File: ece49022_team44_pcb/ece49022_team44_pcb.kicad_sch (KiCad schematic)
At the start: 75 parts, among them J1 Conn_02x05_Odd_Even, J3 Conn_01x05_Female, J4 Conn_01x04_Female, J5 Conn_01x06_Female, Q1 MMBT3904, SW1 RotaryEncoder_Switch, SW2 Reset, U1 STM32F091RCTx, U2 HDC1080, U3 CR2013-MI2120, U4 PCA9306DC, U5 PCF8523T, U6 MAX30102, U7 MPU-6050

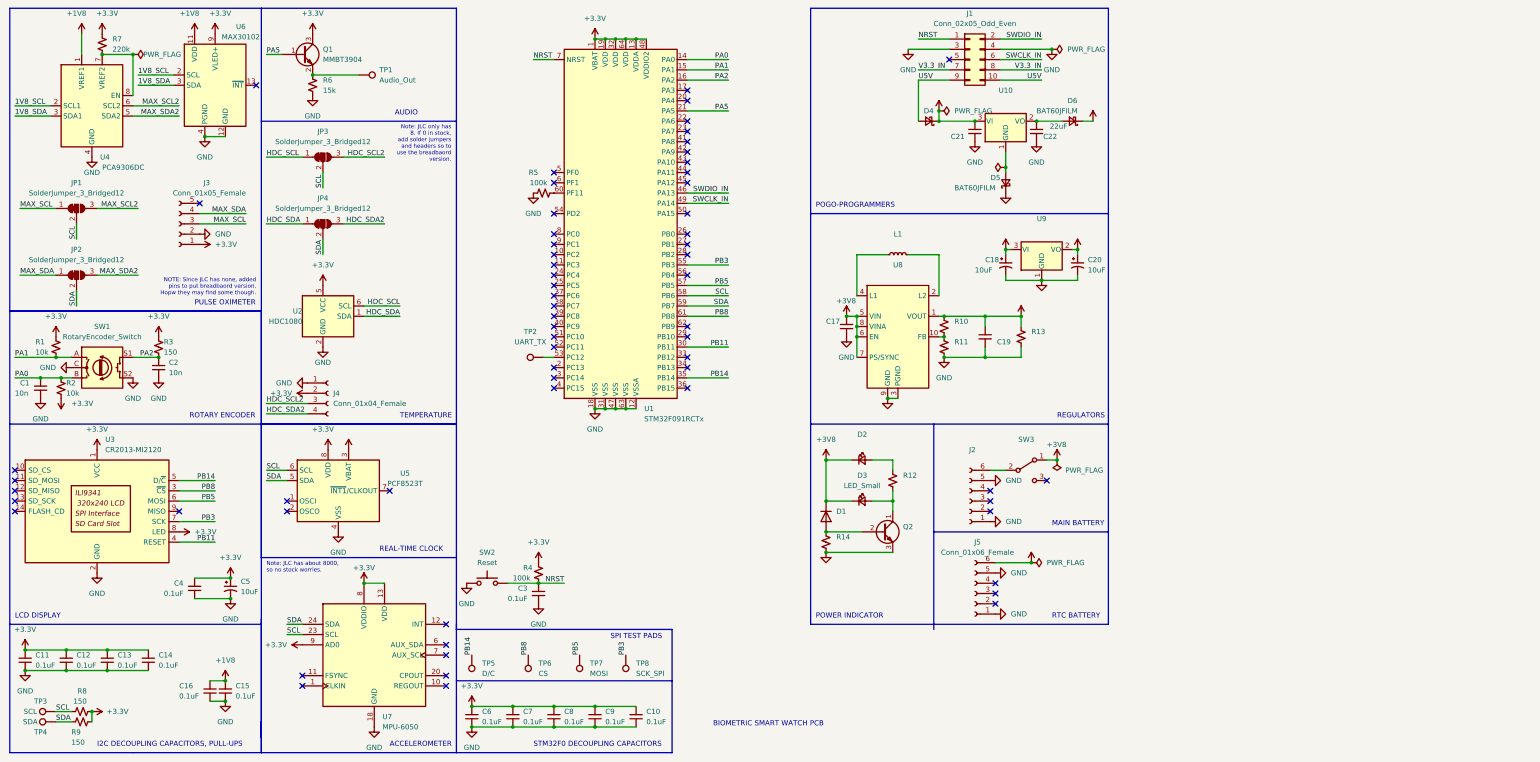
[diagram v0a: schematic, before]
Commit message: All PCB Stuff
Uploaded changes to PCB (fixed the switch and LEDs). Also GERBERs and CENTROIDS, BOM. Checked on JLCPCB, $220 for build and assembly if only 2 boards.

TO-DO:
Double check silk-screen. Make sure comments look fine.
Order PCB when fully reviewed.
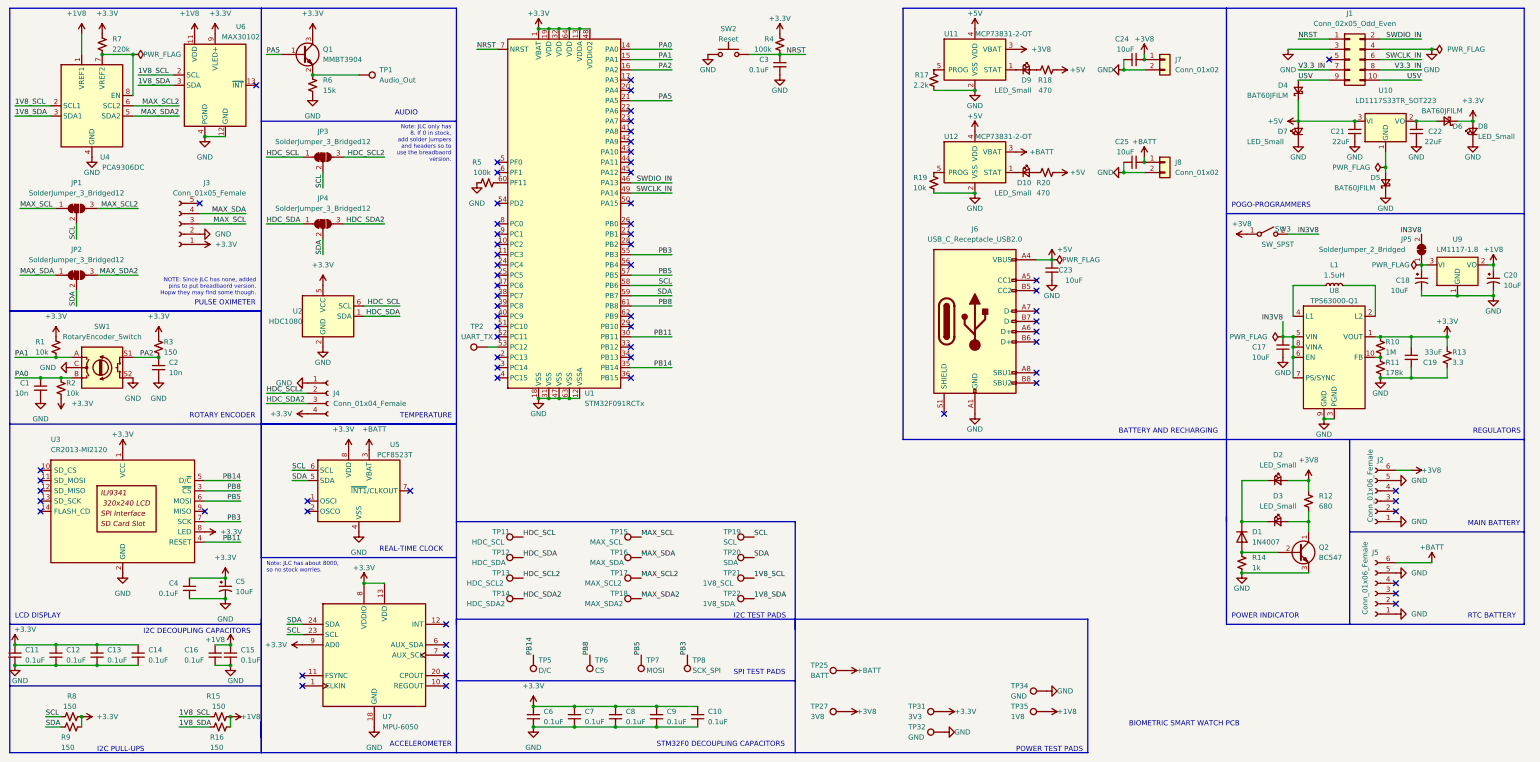
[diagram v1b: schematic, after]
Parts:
- removed SW3: (no value), symbol Switch:SW_SPDT
- removed TP3: SCL, TestPoint:TestPoint_Pad_D2.5mm, symbol Connector:TestPoint
- removed TP4: SDA, TestPoint:TestPoint_Pad_D2.5mm, symbol Connector:TestPoint
- added C23, C24, C25: 10uF, Capacitor_SMD:C_0402_1005Metric, symbol Device:C_Small
- added D10, D7, D8, D9: LED_Small, LED_SMD:LED_0603_1608Metric, symbol Device:LED_Small
- added J6: USB_C_Receptacle_USB2.0, Connector_USB:USB_C_Receptacle_XKB_U262-16XN-4BVC11, symbol Connector:USB_C_Receptacle_USB2.0
- added J7, J8: Conn_01x02, Connector_JST:JST_PH_S2B-PH-K_1x02_P2.00mm_Horizontal, symbol Connector_Generic:Conn_01x02
- added JP5: SolderJumper_2_Bridged, Jumper:SolderJumper-2_P1.3mm_Bridged2Bar_Pad1.0x1.5mm, symbol Jumper:SolderJumper_2_Bridged
- added R15, R16: 150, Resistor_SMD:R_0201_0603Metric, symbol Device:R_Small_US
- added R17: 2.2k, Resistor_SMD:R_0201_0603Metric, symbol Device:R_Small_US
- added R18, R20: 470, Resistor_SMD:R_0201_0603Metric, symbol Device:R_Small_US
- added R19: 10k, Resistor_SMD:R_0201_0603Metric, symbol Device:R_Small_US
- added SW3: SW_SPST, Button_Switch_SMD:SW_DIP_SPSTx01_Slide_Copal_CHS-01B_W7.62mm_P1.27mm, symbol Switch:SW_SPST
- added TP11: HDC_SCL, TestPoint:TestPoint_Pad_D2.5mm, symbol Connector:TestPoint
- added TP12: HDC_SDA, TestPoint:TestPoint_Pad_D2.5mm, symbol Connector:TestPoint
- added TP13: HDC_SCL2, TestPoint:TestPoint_Pad_D2.5mm, symbol Connector:TestPoint
- added TP14: HDC_SDA2, TestPoint:TestPoint_Pad_D2.5mm, symbol Connector:TestPoint
- added TP15: MAX_SCL, TestPoint:TestPoint_Pad_D2.5mm, symbol Connector:TestPoint
- added TP16: MAX_SDA, TestPoint:TestPoint_Pad_D2.5mm, symbol Connector:TestPoint
- added TP17: MAX_SCL2, TestPoint:TestPoint_Pad_D2.5mm, symbol Connector:TestPoint
- added TP18: MAX_SDA2, TestPoint:TestPoint_Pad_D2.5mm, symbol Connector:TestPoint
- added TP19: SCL, TestPoint:TestPoint_Pad_D2.5mm, symbol Connector:TestPoint
- added TP20: SDA, TestPoint:TestPoint_Pad_D2.5mm, symbol Connector:TestPoint
- added TP21: 1V8_SCL, TestPoint:TestPoint_Pad_D2.5mm, symbol Connector:TestPoint
- added TP22: 1V8_SDA, TestPoint:TestPoint_Pad_D2.5mm, symbol Connector:TestPoint
- added TP25: BATT, TestPoint:TestPoint_Pad_D2.5mm, symbol Connector:TestPoint
- added TP27: 3V8, TestPoint:TestPoint_Pad_D2.5mm, symbol Connector:TestPoint
- added TP31: 3V3, TestPoint:TestPoint_Pad_D2.5mm, symbol Connector:TestPoint
- added TP32, TP34: GND, TestPoint:TestPoint_Pad_D2.5mm, symbol Connector:TestPoint
- added TP35: 1V8, TestPoint:TestPoint_Pad_D2.5mm, symbol Connector:TestPoint
- added U11, U12: MCP73831-2-OT, Package_TO_SOT_SMD:SOT-23-5, symbol Battery_Management:MCP73831-2-OT
- C17: value (none) -> 10uF; footprint (none) -> Capacitor_SMD:C_0402_1005Metric; LCSC (none) -> C163694
- C19: value (none) -> 33uF; footprint (none) -> Capacitor_Tantalum_SMD:CP_EIA-3528-21_Kemet-B; LCSC (none) -> C723311
- C21: value (none) -> 22uF; footprint (none) -> Capacitor_SMD:C_0402_1005Metric; LCSC (none) -> C415703
- C22: footprint (none) -> Capacitor_SMD:C_0402_1005Metric; LCSC (none) -> C415703
- D1: value (none) -> 1N4007
- D2: value (none) -> LED_Small; footprint (none) -> LED_SMD:LED_0603_1608Metric; LCSC (none) -> C72043
- D3: footprint (none) -> LED_SMD:LED_0603_1608Metric; LCSC (none) -> C2286
- D4: value (none) -> BAT60JFILM; footprint (none) -> Diode_SMD:D_SOD-323; LCSC (none) -> C133103
- D5, D6: LCSC (none) -> C133103
- J1, TP1, TP2, TP5, TP6, TP7, TP8: now left out of the parts list
- J2: value (none) -> Conn_01x06_Female; footprint (none) -> Connector_PinSocket_2.54mm:PinSocket_1x06_P2.54mm_Vertical; now left out of the parts list
- J5: footprint (none) -> Connector_PinSocket_2.54mm:PinSocket_1x06_P2.54mm_Vertical; now left out of the parts list
- L1: value (none) -> 1.5uH; footprint (none) -> Inductor_SMD:L_0805_2012Metric; LCSC (none) -> C281090
- Q2: value (none) -> BC547; footprint (none) -> Package_TO_SOT_THT:TO-92_Inline; LCSC (none) -> C713613
- R10: value (none) -> 1M; footprint (none) -> Resistor_SMD:R_0402_1005Metric; LCSC (none) -> C26083
- R11: value (none) -> 178k; footprint (none) -> Resistor_SMD:R_0402_1005Metric; LCSC (none) -> C185459
- R12: value (none) -> 680; footprint (none) -> Resistor_SMD:R_0201_0603Metric; LCSC (none) -> C473509
- R13: value (none) -> 3.3; footprint (none) -> Resistor_SMD:R_0603_1608Metric; LCSC (none) -> C22979
- R14: value (none) -> 1k; footprint (none) -> Resistor_SMD:R_0201_0603Metric; LCSC (none) -> C102683
- R7: footprint Resistor_SMD:R_0201_0603Metric -> Resistor_SMD:R_0603_1608Metric; LCSC (none) -> C22961
- U10: value (none) -> LD1117S33TR_SOT223; footprint (none) -> Package_TO_SOT_SMD:SOT-223-3_TabPin2; LCSC (none) -> C35879
- U8: value (none) -> TPS63000-Q1; footprint (none) -> Package_SON:Texas_DRC0010J_ThermalVias
- U9: value (none) -> LM1117-1.8; footprint (none) -> Package_TO_SOT_SMD:TO-252-2
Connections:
- net +1V8: now also R15.1, R16.2, TP35.1
- net +3V3: now also J4.4 (Pin_4), D8.2 (A), TP31.1; no longer J4.2 (Pin_2)
- net +3V8: now also D2.2 (A), J2.6 (Pin_6), R12.1, C24.1, J7.1 (Pin_1), SW3.1 (A), TP27.1, U11.3 (VBAT); no longer C17.2, C18.1, D1.2 (K), D2.1 (K), D3.1 (K), U8.5 (VIN), U8.6 (EN), U8.7 (PS/SYNC), U8.8 (VINA), U9.3 (VI)
- net +5V: now also C23.1, D7.2 (A), J6.A4 (VBUS), J6.A9 (VBUS), J6.B4 (VBUS), J6.B9 (VBUS), R18.2, R20.1, U11.4 (VDD), U12.4 (VDD)
- net +BATT: now also C25.1, J8.1 (Pin_1), TP25.1, U12.3 (VBAT)
- net 1V8_SCL: now also R15.2, TP21.1
- net 1V8_SDA: now also R16.1, TP22.1
- net GND: now also C23.2, C24.2, C25.2, D7.1 (K), D8.1 (K), J6.A1 (GND), J6.A12 (GND), J6.B1 (GND), J6.B12 (GND), J7.2 (Pin_2), J8.2 (Pin_2), R17.1, R19.1, TP32.1, TP34.1, U11.2 (VSS), U12.2 (VSS)
- net HDC_SCL: now also TP11.1
- net HDC_SCL2: now also J4.2 (Pin_2), TP13.1; no longer J4.3 (Pin_3)
- net HDC_SDA: now also TP12.1
- net HDC_SDA2: now also J4.3 (Pin_3), TP14.1; no longer J4.4 (Pin_4)
- net MAX_SCL: now also TP15.1
- net MAX_SCL2: now also TP17.1
- net MAX_SDA: now also TP16.1
- net MAX_SDA2: now also TP18.1
- net SCL: now also TP19.1
- net SDA: now also TP20.1
- new net: C18.1, JP5.1 (A), U9.3 (VI)
- new net: D9.2 (A), R18.1
- new net: D10.1 (K), U12.1 (STAT)
- new net: R19.2, U12.5 (PROG)
- new net: D1.2 (K), D2.1 (K), D3.1 (K)
- new net: R17.2, U11.5 (PROG)
- new net: D9.1 (K), U11.1 (STAT)
- new net: D10.2 (A), R20.2
- new net IN3V8: C17.2, JP5.2 (B), SW3.2 (B), U8.5 (VIN), U8.6 (EN), U8.7 (PS/SYNC), U8.8 (VINA)
- no-connect marks 63 -> 71
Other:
- note added: "BATTERY AND RECHARGING"
- note added: "I2C DECOUPLING CAPACITORS"
- note added: "I2C PULL-UPS"
- note added: "I2C TEST PADS"
- note added: "POWER TEST PADS"
- note removed: "I2C DECOUPLING CAPACITORS, PULL-UPS"
- moved on the sheet: C10, C11, C12, C13, C14, C15, C16, C17, C18, C19, C20, C21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
